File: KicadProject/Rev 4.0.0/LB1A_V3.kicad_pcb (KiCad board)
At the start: 6 copper layers, 42 x 42 mm, 187 parts, among them J601 2337019-1, J602 2337019-1, U101 STM32MP157CAA3, U201 AS4C256M16D3LC-12BCN, U401 STPMIC1xPQR, U501 S40FC004C1B2C00000, U601 LBEE59B1LV-278, U701 DF40C-70DP-0.4V(51), U702 DF40C-100DP-0.4V(51), U703 DF40C-100DP-0.4V(51), X101 32.768kHz, Y101 24MHz

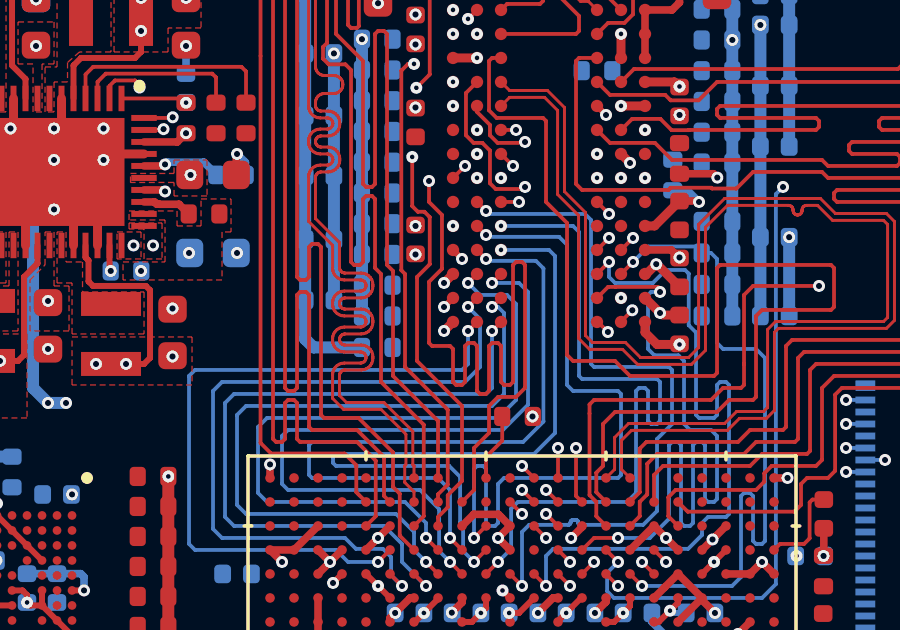
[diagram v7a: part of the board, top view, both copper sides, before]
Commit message: pull up resistors left
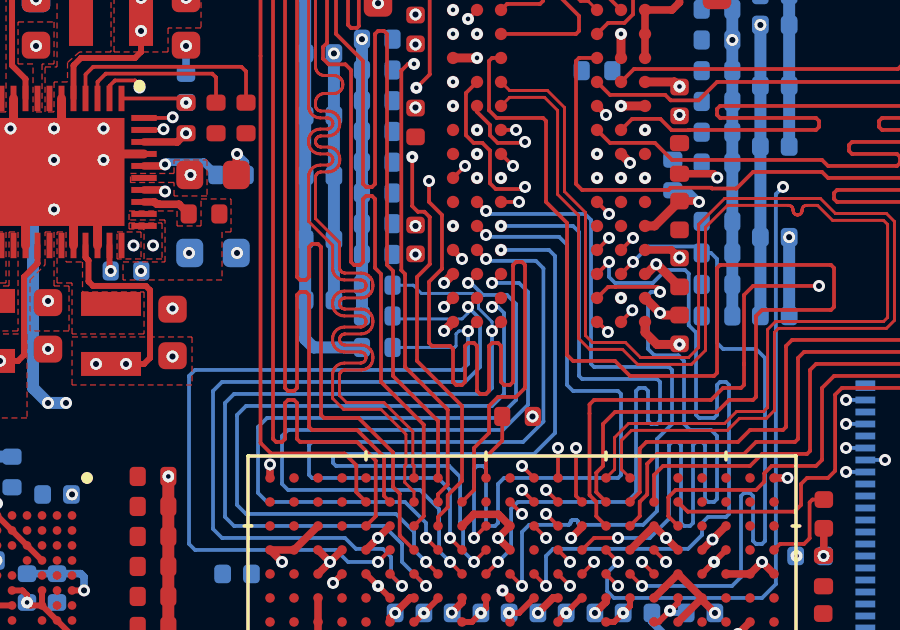
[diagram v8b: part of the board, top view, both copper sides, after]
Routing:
- net /MPU_DDR3L_Memory/DDR_A13: track 23.8 -> 28.1 mm
- net /MPU_DDR3L_Memory/DDR_RESETN: track 23.7 -> 26.7 mm
- net /MPU_DDR3L_Memory/DDR_A7: track 24.4 -> 27.3 mm
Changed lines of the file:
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@@
     (thickness 1.2)
     (drawings 8)
-    (tracks 2738)
+    (tracks 2756)
     (zones 0)
     (modules 187)
@@
     (0 L1_Sig_Pwr.Cu mixed hide)
     (1 L2_Gnd.Cu power hide)
-    (2 L3_Sig_Pwr.Cu mixed)
-    (3 L4_Sig_Gnd.Cu mixed)
+    (2 L3_Sig_Pwr.Cu mixed hide)
+    (3 L4_Sig_Gnd.Cu mixed hide)
     (4 L5_Gnd_Pwr.Cu power hide)
-    (31 L6_Sig_Pwr.Cu mixed hide)
+    (31 L6_Sig_Pwr.Cu mixed)
     (32 B.Adhes user hide)
     (33 F.Adhes user hide)
@@
   )
   (setup
-    (last_trace_width 0.127)
+    (last_trace_width 0.1)
     (user_trace_width 0.1)
     (user_trace_width 0.127)
@@
   (via (at 196.1 100.9) (size 0.4) (drill 0.2) (layers L1_Sig_Pwr.Cu L6_Sig_Pwr.Cu) (net 43))
   (segment (start 196.4 100.6) (end 196.1 100.9) (width 0.127) (layer L1_Sig_Pwr.Cu) (net 43))
+  (segment (start 194.7 108.9) (end 194.7 109.4) (width 0.127) (layer L6_Sig_Pwr.Cu) (net 43))
+  (segment (start 189.4 108.2) (end 194 108.2) (width 0.127) (layer L6_Sig_Pwr.Cu) (net 43))
   (segment (start 189.1 105.7) (end 189.1 107.9) (width 0.127) (layer L6_Sig_Pwr.Cu) (net 43))
+  (segment (start 194 108.2) (end 194.7 108.9) (width 0.127) (layer L6_Sig_Pwr.Cu) (net 43))
   (segment (start 189.4 105.4) (end 189.1 105.7) (width 0.127) (layer L6_Sig_Pwr.Cu) (net 43))
-  (segment (start 194.7 108.9) (end 194.7 109.4) (width 0.127) (layer L6_Sig_Pwr.Cu) (net 43))
-  (segment (start 189.1 107.9) (end 189.4 108.2) (width 0.127) (layer L6_Sig_Pwr.Cu) (net 43))
   (segment (start 197.7 104.8) (end 197.1 105.4) (width 0.127) (layer L6_Sig_Pwr.Cu) (net 43))
   (segment (start 197.7 101.6) (end 197.7 104.8) (width 0.127) (layer L6_Sig_Pwr.Cu) (net 43))
-  (segment (start 194 108.2) (end 194.7 108.9) (width 0.127) (layer L6_Sig_Pwr.Cu) (net 43))
-  (segment (start 189.4 108.2) (end 194 108.2) (width 0.127) (layer L6_Sig_Pwr.Cu) (net 43))
   (segment (start 197.1 105.4) (end 189.4 105.4) (width 0.127) (layer L6_Sig_Pwr.Cu) (net 43))
+  (segment (start 196.6 101.3) (end 197.4 101.3) (width 0.127) (layer L6_Sig_Pwr.Cu) (net 43))
+  (segment (start 189.1 107.9) (end 189.4 108.2) (width 0.127) (layer L6_Sig_Pwr.Cu) (net 43))
+  (segment (start 196.2 100.9) (end 196.6 101.3) (width 0.127) (layer L6_Sig_Pwr.Cu) (net 43))
   (segment (start 197.4 101.3) (end 197.7 101.6) (width 0.127) (layer L6_Sig_Pwr.Cu) (net 43))
-  (segment (start 196.5 101.3) (end 197.4 101.3) (width 0.127) (layer L6_Sig_Pwr.Cu) (net 43))
-  (segment (start 196.1 100.9) (end 196.5 101.3) (width 0.127) (layer L6_Sig_Pwr.Cu) (net 43))
+  (segment (start 196.1 100.9) (end 196.2 100.9) (width 0.127) (layer L6_Sig_Pwr.Cu) (net 43))
   (via (at 201.2 101.4) (size 0.4) (drill 0.15) (layers L1_Sig_Pwr.Cu L6_Sig_Pwr.Cu) (net 44))
   (via (at 202.7 110.2) (size 0.4) (drill 0.2) (layers L1_Sig_Pwr.Cu L6_Sig_Pwr.Cu) (net 44))
@@
   (segment (start 193.536499 110.636499) (end 193.536499 110.036499) (width 0.127) (layer L6_Sig_Pwr.Cu) (net 45))
   (segment (start 193.9 111) (end 193.536499 110.636499) (width 0.127) (layer L6_Sig_Pwr.Cu) (net 45))
+  (segment (start 196.1 101.7) (end 196.1 101.9) (width 0.1) (layer L6_Sig_Pwr.Cu) (net 45))
+  (segment (start 196.1 101.9) (end 195.9 102.1) (width 0.1) (layer L6_Sig_Pwr.Cu) (net 45))
+  (segment (start 193.685 102.1) (end 193.585 102) (width 0.1) (layer L6_Sig_Pwr.Cu) (net 45))
+  (segment (start 195.9 102.1) (end 193.685 102.1) (width 0.1) (layer L6_Sig_Pwr.Cu) (net 45))
   (segment (start 196.7 107.400001) (end 196.7 106.7) (width 0.127) (layer L1_Sig_Pwr.Cu) (net 46))
   (segment (start 197.24 106.16) (end 197.24 105.35) (width 0.127) (layer L1_Sig_Pwr.Cu) (net 46))
@@
   (segment (start 196.9 104.4) (end 196.7 104.6) (width 0.127) (layer L6_Sig_Pwr.Cu) (net 52))
   (segment (start 196.9 102.5) (end 196.9 104.4) (width 0.127) (layer L6_Sig_Pwr.Cu) (net 52))
+  (segment (start 194.275 100.975) (end 193.585 100.975) (width 0.1) (layer L6_Sig_Pwr.Cu) (net 52))
+  (segment (start 194.550001 101.250001) (end 194.275 100.975) (width 0.1) (layer L6_Sig_Pwr.Cu) (net 52))
+  (segment (start 196.248053 101.250001) (end 194.550001 101.250001) (width 0.1) (layer L6_Sig_Pwr.Cu) (net 52))
+  (segment (start 196.450001 101.451949) (end 196.248053 101.250001) (width 0.1) (layer L6_Sig_Pwr.Cu) (net 52))
+  (segment (start 196.450001 101.748053) (end 196.450001 101.451949) (width 0.1) (layer L6_Sig_Pwr.Cu) (net 52))
+  (segment (start 196.9 102.198052) (end 196.450001 101.748053) (width 0.1) (layer L6_Sig_Pwr.Cu) (net 52))
+  (segment (start 196.9 102.5) (end 196.9 102.198052) (width 0.1) (layer L6_Sig_Pwr.Cu) (net 52))
   (via (at 200.3 110.2) (size 0.4) (drill 0.2) (layers L1_Sig_Pwr.Cu L6_Sig_Pwr.Cu) (net 53))
   (segment (start 199.9 110.6) (end 200.3 110.2) (width 0.127) (layer L1_Sig_Pwr.Cu) (net 53))
@@
   (segment (start 187 103.8) (end 195.9 103.8) (width 0.127) (layer L6_Sig_Pwr.Cu) (net 57))
   (segment (start 193.1 110.2) (end 192.1 110.2) (width 0.127) (layer L6_Sig_Pwr.Cu) (net 57))
+  (segment (start 193.585 103.05) (end 194.35 103.05) (width 0.1) (layer L6_Sig_Pwr.Cu) (net 57))
+  (segment (start 196.1 102.5) (end 195.8 102.5) (width 0.1) (layer L6_Sig_Pwr.Cu) (net 57))
+  (segment (start 195.8 102.5) (end 195.7 102.6) (width 0.1) (layer L6_Sig_Pwr.Cu) (net 57))
+  (segment (start 195.7 102.6) (end 195.7 103) (width 0.1) (layer L6_Sig_Pwr.Cu) (net 57))
+  (segment (start 195.65 103.05) (end 194.35 103.05) (width 0.1) (layer L6_Sig_Pwr.Cu) (net 57))
+  (segment (start 195.7 103) (end 195.65 103.05) (width 0.1) (layer L6_Sig_Pwr.Cu) (net 57))
   (via (at 202 97.4) (size 0.4) (drill 0.15) (layers L1_Sig_Pwr.Cu L6_Sig_Pwr.Cu) (net 58))
   (via (at 201.1 110.2) (size 0.4) (drill 0.2) (layers L1_Sig_Pwr.Cu L6_Sig_Pwr.Cu) (net 58))
